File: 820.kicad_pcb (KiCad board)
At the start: 4 copper layers, 48 x 105 mm, 125 parts, among them J1 PJ301BM, J10 PJ301BM, J2 PJ301BM, J4 PJ301BM, J5 PJ301BM, J6 PJ301BM, J7 PJ301BM, J8 PJ301BM, J9 PJ301BM, P1 CONN_02X05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

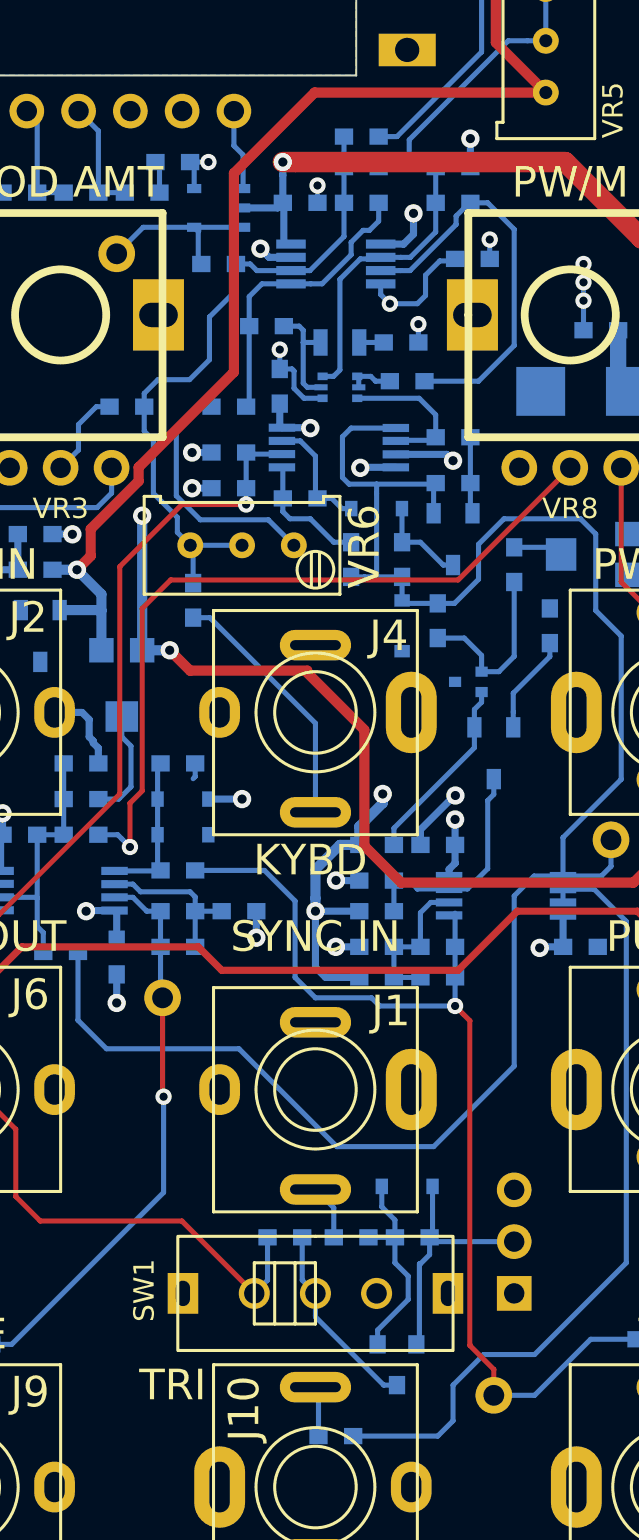
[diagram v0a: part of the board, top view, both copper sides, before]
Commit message: updates for final prototype, changed matched pair back to SOT-363
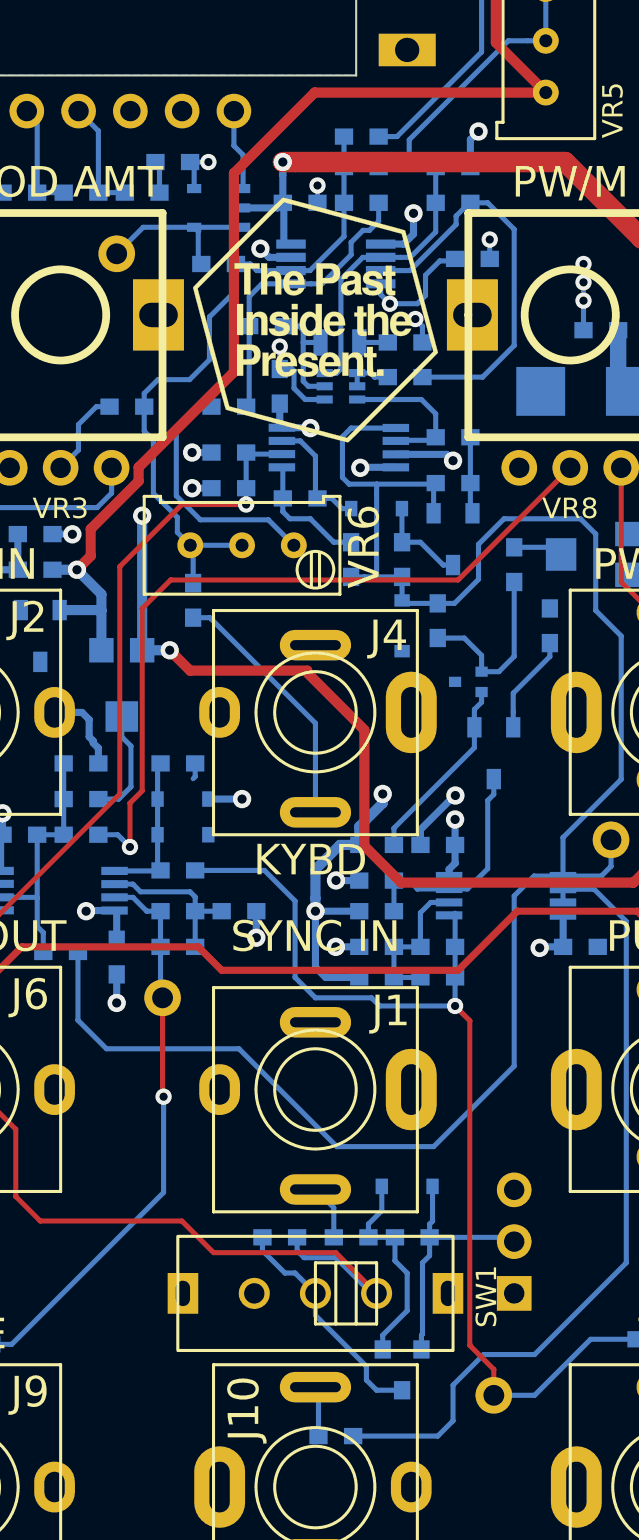
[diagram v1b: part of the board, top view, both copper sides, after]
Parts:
- added G***: LOGO, LOGO, F.Cu at (116.0, 80.5)
- added G***: LOGO, LOGO, B.Cu at (128.8, 41.2)
- Q1: footprint TO_SOT_Packages_SMD:SOT-666 -> MyModules:SOT363-JRL
- R16: value 91K -> 82K
- R17: value 56K -> 27K
- moved G*** 12.0 mm to (133.5, 125.3)
- moved Q2 0.35 mm to (120.2, 132.0)
- moved R9 0.25 mm to (114.2, 125.5), turned to 0 degrees
- moved R19 0.22 mm to (120.4, 83.3)
- moved R14 0.20 mm to (120.4, 81.6)
- moved Q1 0.07 mm to (117.2, 83.8), turned to 90 degrees
- turned SW1 to 180 degrees
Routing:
- net SYNC: track 68.0 -> 76.6 mm
- net Net-(Q2-Pad3): track 9.56 -> 11.4 mm
- net GND: track 46.4 -> 47.1 mm
- net Net-(D5-Pad2): track 12.3 -> 13.0 mm
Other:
- board text added: "GND"
- board text added: "SAW"
- board text added: "STRIPE"
- board text added: "−12 V"
- board text removed: "820 VCO"

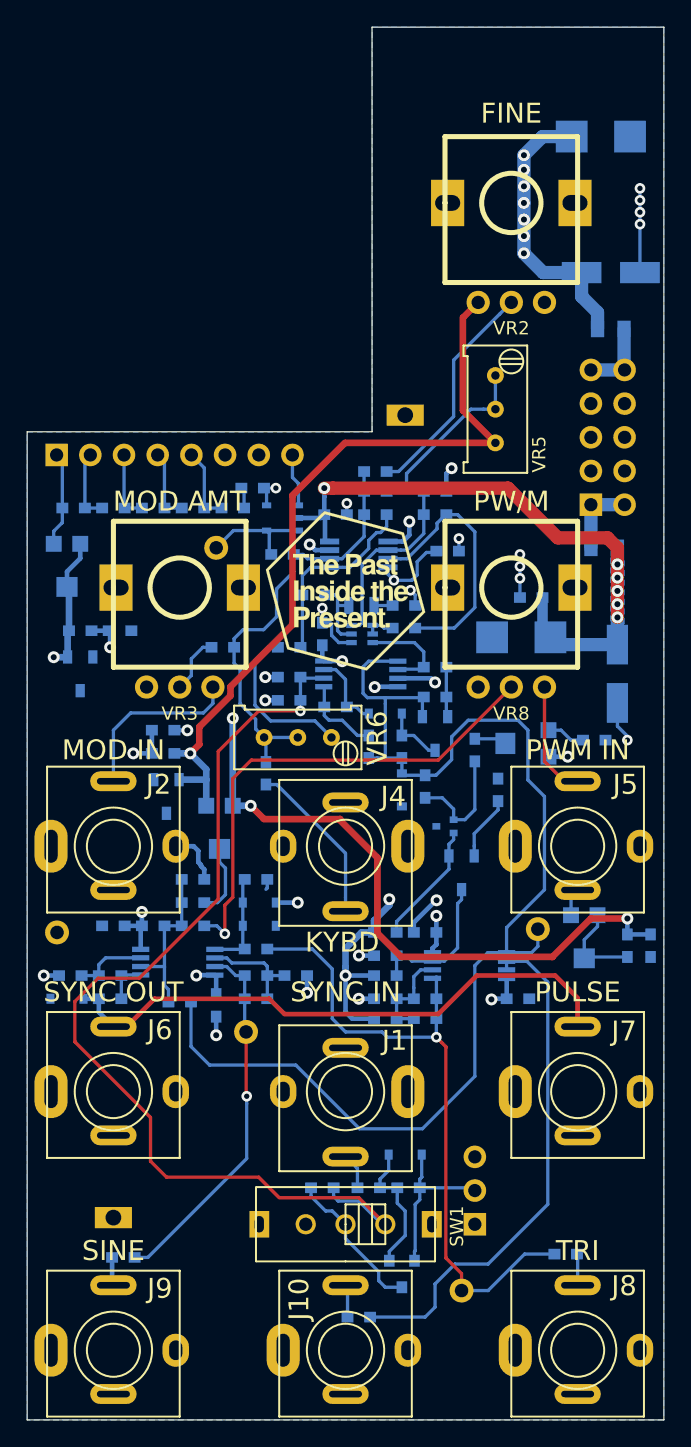
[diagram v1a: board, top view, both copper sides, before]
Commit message: gerbers ready to submit to pcb fab house. need to generate gerbers for rotary switch board still
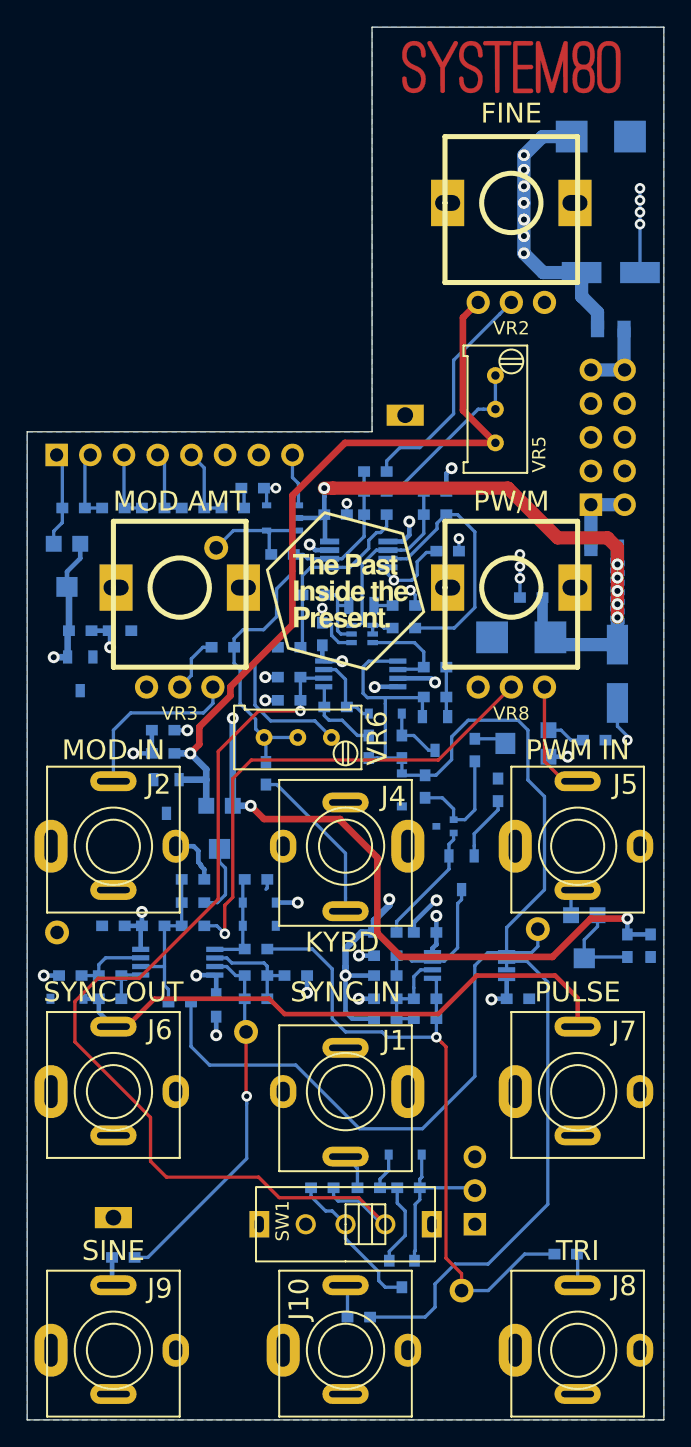
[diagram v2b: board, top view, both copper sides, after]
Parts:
- added G***: LOGO, LOGO, F.Cu at (128.5, 41.0)
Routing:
- net Net-(R15-Pad1): track 13.9 -> 13.3 mm

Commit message: final prototype ordred, built and tested, committing now and then branching to panelization
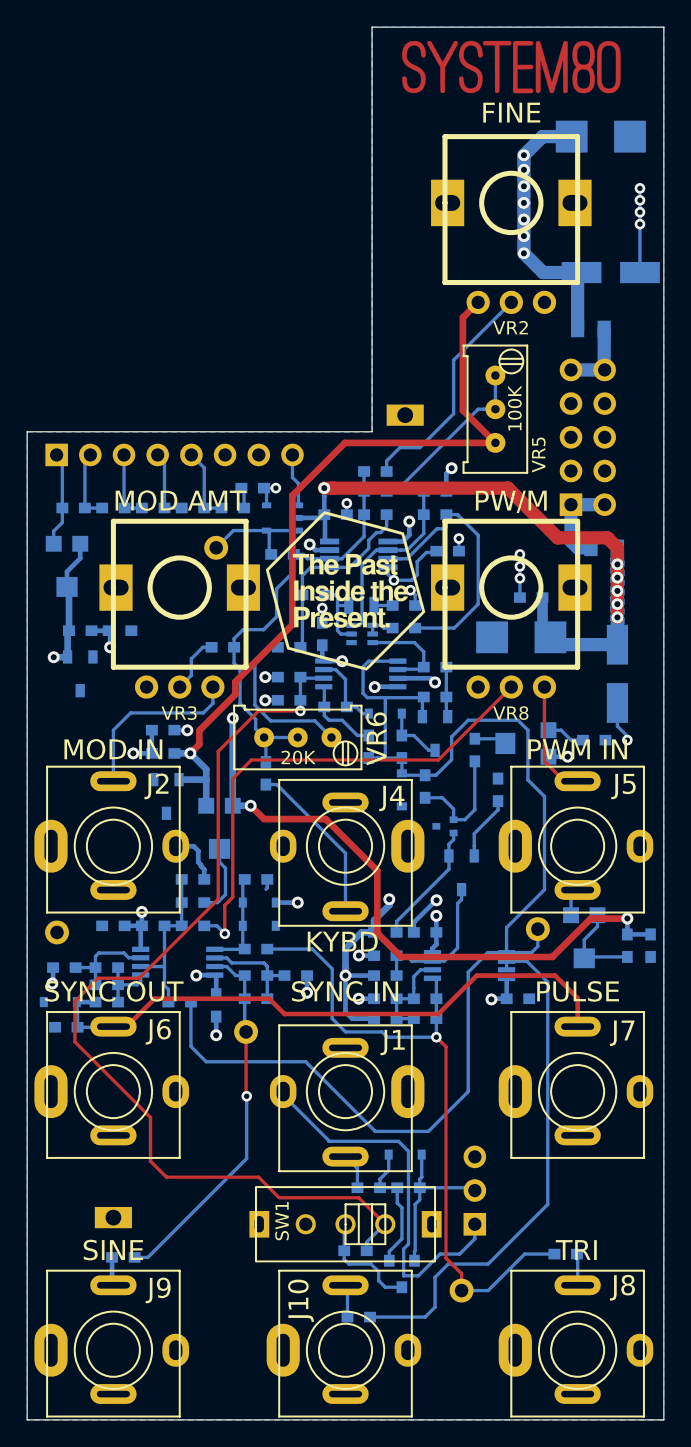
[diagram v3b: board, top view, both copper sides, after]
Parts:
- added C22: 100p, MyModules:SM0603-C-MURATA, B.Cu at (98.0, 110.2)
- added G***: LOGO, w_logo:Logo_silk_WEEE_3.4x5mm, B.Cu at (107.1, 139.9)
- added G***: LOGO, w_logo:Logo_silk_CE_5x3.6mm, B.Cu at (124.5, 138.0)
- added G***: LOGO, w_logo:Logo_silk_ROHS_5x2.8mm, B.Cu at (124.4, 141.2)
- added R51: 33K, MyModules:SM0603-R-YAGEO, B.Cu at (95.0, 113.4)
- R41: value 1K -> 4.7K
- moved R9 5.37 mm to (116.8, 130.2)
- moved F1 1.50 mm to (134.5, 60.8)
- moved P1 1.50 mm to (133.0, 74.0)
- moved R32 0.75 mm to (94.8, 108.9)
- moved R38 0.65 mm to (98.0, 108.9)
- moved D10 0.56 mm to (94.5, 111.5)
- moved R41 0.35 mm to (98.0, 111.5)
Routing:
- net GND: track 47.1 -> 72.5 mm
- net Net-(Q2-Pad3): track 11.4 -> 8.31 mm
- net /PULSE: track 53.6 -> 55.9 mm
- net SYNC: track 76.6 -> 74.4 mm
- net Net-(C22-Pad1): track 5.49 -> 7.31 mm
- net Net-(C22-Pad2): track 3.22 -> 4.96 mm
- net +10V: track 123.4 -> 124.8 mm
- net Net-(F2-Pad1): track 5.79 -> 7.00 mm
- net +12V: track 220.3 -> 219.5 mm
- net Net-(C17-Pad2): track 94.2 -> 94.7 mm
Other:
- board text added: "r1.2 04/2019"
- board text removed: "r1.1 03/2019"
